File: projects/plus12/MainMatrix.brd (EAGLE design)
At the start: 114.3 x 92.7 mm, 41 parts, among them SW1 RSTSWSMD, SW2 TRANSFERPADDY

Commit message: Getting ready for pictures
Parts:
- added U$1: (no value), Logos:3_8INCH_BOT
- added U$2: (no value), Logos:3_8INCH_TOP
- INT1: value INTRCNNT -> INTRCNNT4X2; device Keys:INTRCNNT -> Keys:INTRRIBBON
- moved D11 33.0 mm to (127.6, 80.0)
- moved D5 33.0 mm to (127.6, 99.1)
- moved D4 26.3 mm to (117.5, 70.5), turned to 90 degrees
- moved UC1 19.0 mm to (108.0, 114.3)
- moved D18 14.6 mm to (146.7, 59.1)
- moved D12 14.6 mm to (146.7, 78.1)
- moved D6 14.6 mm to (146.7, 97.2)
- moved SWI18 14.6 mm to (146.1, 49.5)
- moved SWI12 14.6 mm to (146.1, 68.6)
- moved SWI6 14.6 mm to (146.1, 87.6)
- moved SWI11 14.0 mm to (127.0, 70.5)
- moved SWI17 14.0 mm to (127.0, 51.4)
- moved SWI5 14.0 mm to (127.0, 89.5)
- moved D15 12.2 mm to (98.4, 68.6), turned to 90 degrees
- moved D17 10.5 mm to (127.0, 61.0), turned to 0 degrees
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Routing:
- net N$33: track 122.7 -> 47.0 mm, vias 1 -> 0
- net N$25: track 162.7 -> 96.6 mm
- net N$21: track 198.3 -> 152.5 mm
- net N$26: track 150.1 -> 105.8 mm
- net N$5: track 18.4 -> 62.7 mm, vias 0 -> 1
- net N$35: track 91.8 -> 50.0 mm
- net N$20: track 157.7 -> 197.7 mm, vias 2 -> 1
- net N$22: track 190.6 -> 152.4 mm
- net N$18: track 39.1 -> 12.4 mm
- net N$23: track 162.6 -> 137.5 mm, vias 2 -> 1
- net N$32: track 72.6 -> 50.1 mm
- net N$12: track 36.5 -> 14.6 mm
- net N$28: track 65.9 -> 45.9 mm
- net N$24: track 147.8 -> 136.3 mm, vias 1 -> 0
- net N$1: track 120.4 -> 109.5 mm, vias 2 -> 0
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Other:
- board size 114.3 x 92.7 mm -> 114.3 x 78.1 mm
- board text added: "Designed by Dotdash32"
- board text added: "Plus12 Mainland"

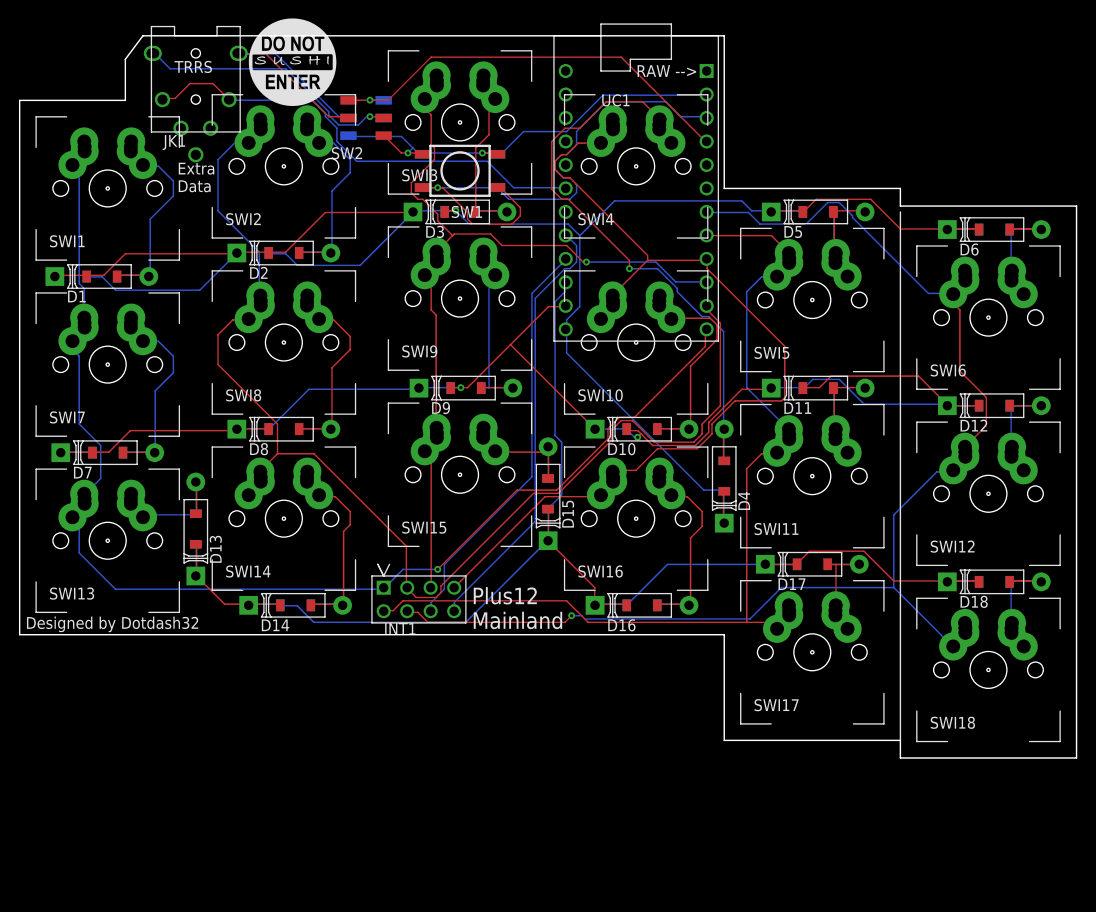
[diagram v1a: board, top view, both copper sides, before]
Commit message: Adding low profile support
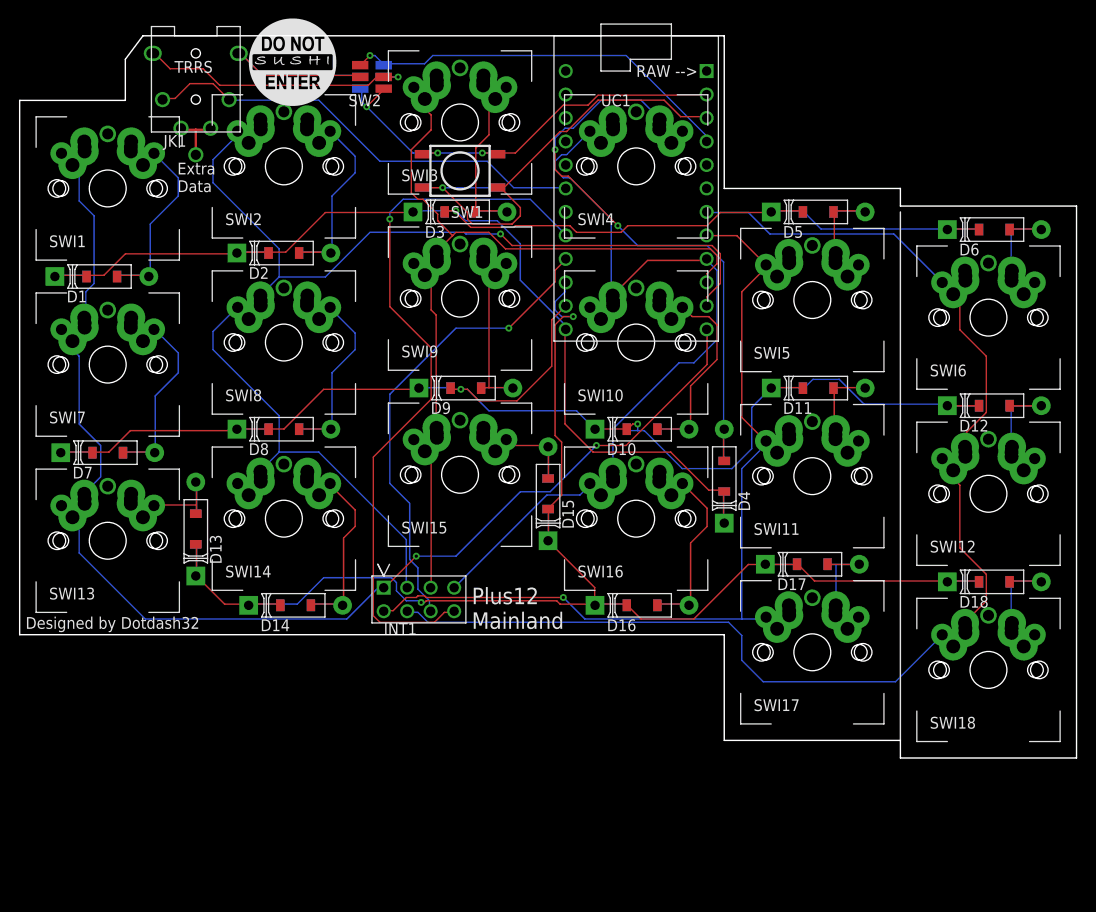
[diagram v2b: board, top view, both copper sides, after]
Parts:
- JK1: value TRRSJACK -> TRRSJACKUNDER
- moved SW2 4.49 mm to (79.4, 113.7)
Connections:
- net N$1: now also SWI11.LLP, SWI17.LLP, SWI5.LLP
- net N$10: now also SWI9.RLP
- net N$11: now also SWI10.RLP
- net N$12: now also SWI11.RLP
- net N$13: now also SWI12.RLP
- net N$14: now also SWI13.RLP
- net N$15: now also SWI14.RLP
- net N$16: now also SWI15.RLP
- net N$17: now also SWI16.RLP
- net N$18: now also SWI17.RLP
- net N$19: now also SWI18.RLP
- net N$2: now also SWI1.RLP
- net N$23: now also SWI1.LLP, SWI13.LLP, SWI7.LLP
- net N$24: now also SWI14.LLP, SWI2.LLP, SWI8.LLP
- net N$25: now also SWI15.LLP, SWI3.LLP, SWI9.LLP
- net N$26: now also SWI10.LLP, SWI16.LLP, SWI4.LLP
- net N$27: now also SWI12.LLP, SWI18.LLP, SWI6.LLP
- net N$3: now also SWI2.RLP
- net N$4: now also SWI3.RLP
- net N$5: now also SWI4.RLP
- net N$6: now also SWI5.RLP
- net N$7: now also SWI6.RLP
- net N$8: now also SWI7.RLP
- net N$9: now also SWI8.RLP
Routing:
- net N$33: track 47.0 -> 78.8 mm, vias 0 -> 1
- net N$20: track 197.7 -> 179.3 mm
- net N$5: track 62.7 -> 71.5 mm, vias 1 -> 2
- net N$23: track 137.5 -> 145.6 mm, vias 1 -> 2
- net N$25: track 96.6 -> 104.5 mm, vias 1 -> 0
- net N$7: track 11.5 -> 19.0 mm
- net N$34: track 60.1 -> 52.8 mm
- net N$29: track 44.1 -> 51.2 mm, vias 0 -> 1
- net N$22: track 152.4 -> 159.3 mm, vias 0 -> 2
- net N$19: track 11.6 -> 18.3 mm
- net N$13: track 12.0 -> 18.2 mm
- net N$24: track 136.3 -> 142.4 mm, vias 0 -> 1
- net N$15: track 21.7 -> 27.7 mm
- net N$8: track 22.2 -> 28.2 mm
- net N$17: track 22.1 -> 28.1 mm
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
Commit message: more updates than should be in one commit, lots of work
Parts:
- moved SW1 13.5 mm to (79.4, 94.0), turned to 270 degrees
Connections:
- new net N$36: JK1.3B, JK1.3T, JK1.EXTRA_DATA
- net N$1: now also SWI11.LRLP, SWI17.LRLP, SWI5.LRLP
- net N$10: now also SWI9.RLMID; no longer SWI9.RLP
- net N$11: now also SWI10.RLMID; no longer SWI10.RLP
- net N$12: now also SWI11.RLMID; no longer SWI11.RLP
- net N$13: now also SWI12.RLMID; no longer SWI12.RLP
- net N$14: now also SWI13.RLMID; no longer SWI13.RLP
- net N$15: now also SWI14.RLMID; no longer SWI14.RLP
- net N$16: now also SWI15.RLMID; no longer SWI15.RLP
- net N$17: now also SWI16.RLMID; no longer SWI16.RLP
- net N$18: now also SWI17.RLMID; no longer SWI17.RLP
- net N$19: now also SWI18.RLMID; no longer SWI18.RLP
- net N$2: now also SWI1.RLMID; no longer SWI1.RLP
- net N$23: now also SWI1.LRLP, SWI13.LRLP, SWI7.LRLP
- net N$24: now also SWI14.LRLP, SWI2.LRLP, SWI8.LRLP
- net N$25: now also SWI15.LRLP, SWI3.LRLP, SWI9.LRLP
- net N$26: now also SWI10.LRLP, SWI16.LRLP, SWI4.LRLP
- net N$27: now also SWI12.LRLP, SWI18.LRLP, SWI6.LRLP
- net N$3: now also SWI2.RLMID; no longer SWI2.RLP
- net N$4: now also SWI3.RLMID; no longer SWI3.RLP
- net N$5: now also SWI4.RLMID; no longer SWI4.RLP
- net N$6: now also SWI5.RLMID; no longer SWI5.RLP
- net N$7: now also SWI6.RLMID; no longer SWI6.RLP
- net N$8: now also SWI7.RLMID; no longer SWI7.RLP
- net N$9: now also SWI8.RLMID; no longer SWI8.RLP
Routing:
- net N$23: track 145.6 -> 190.9 mm, vias 2 -> 0
- net N$27: track 149.0 -> 181.3 mm
- net N$33: track 78.8 -> 46.9 mm, vias 1 -> 0
- net N$1: track 109.8 -> 140.7 mm, vias 1 -> 0
- net N$25: track 104.5 -> 132.9 mm
- net N$24: track 142.4 -> 167.5 mm, vias 1 -> 0
- net N$35: track 50.0 -> 73.1 mm
- net N$5: track 71.5 -> 49.8 mm, vias 2 -> 0
- net N$22: track 159.3 -> 174.5 mm, vias 2 -> 0
- net N$31: track 29.3 -> 16.3 mm, vias 0 -> 1
- net N$21: track 150.2 -> 137.4 mm, vias 2 -> 1
- net N$16: track 16.7 -> 28.1 mm
- net N$14: track 16.5 -> 26.7 mm
- net N$20: track 179.3 -> 189.4 mm, vias 1 -> 2
- net N$26: track 100.7 -> 110.4 mm
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
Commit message: more updates than should be in one commit, lots of work
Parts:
- moved D4 30.3 mm to (127.6, 99.1), turned to 0 degrees
- moved D11 19.1 mm to (127.6, 61.0)
- moved D5 19.0 mm to (127.6, 80.0)
- moved D17 9.71 mm to (117.5, 62.9), turned to 90 degrees
- moved SW2 4.49 mm to (78.7, 109.2)
- moved D15 0.64 mm to (98.4, 67.9)
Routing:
- net N$21: track 137.4 -> 199.0 mm, vias 1 -> 4
- net N$20: track 189.4 -> 158.7 mm
- net N$23: track 190.9 -> 166.3 mm
- net N$22: track 174.5 -> 156.7 mm
- net N$18: track 26.6 -> 44.0 mm
- net N$31: track 16.3 -> 31.6 mm, vias 1 -> 0
- net N$24: track 167.5 -> 152.7 mm
- net N$25: track 132.9 -> 120.0 mm
- net N$34: track 54.6 -> 65.6 mm
- net N$35: track 73.1 -> 63.6 mm
- net N$5: track 49.8 -> 44.7 mm, vias 0 -> 1
- net N$33: track 46.9 -> 50.8 mm
- net N$12: track 27.4 -> 25.4 mm
- net N$6: track 27.0 -> 25.1 mm
- net N$26: track 110.4 -> 111.6 mm
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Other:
- outline, holes or cut-outs redrawn
